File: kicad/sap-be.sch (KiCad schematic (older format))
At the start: 0 parts

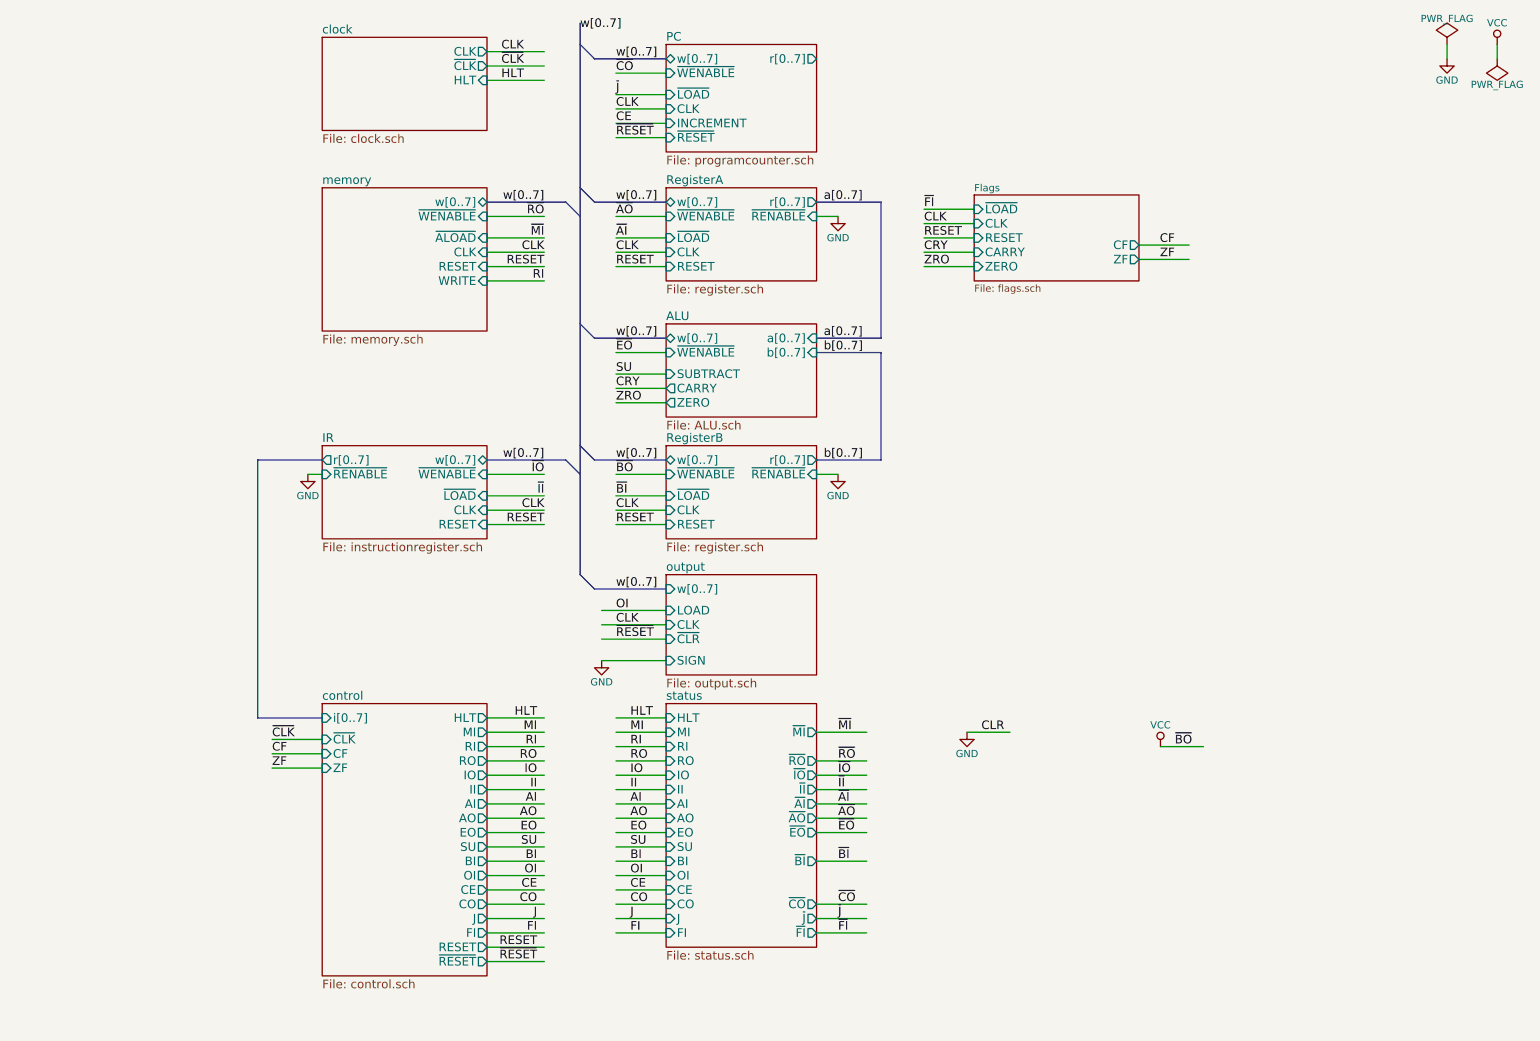
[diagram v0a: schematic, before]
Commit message: Update bugfix version to use updated kicad libraries
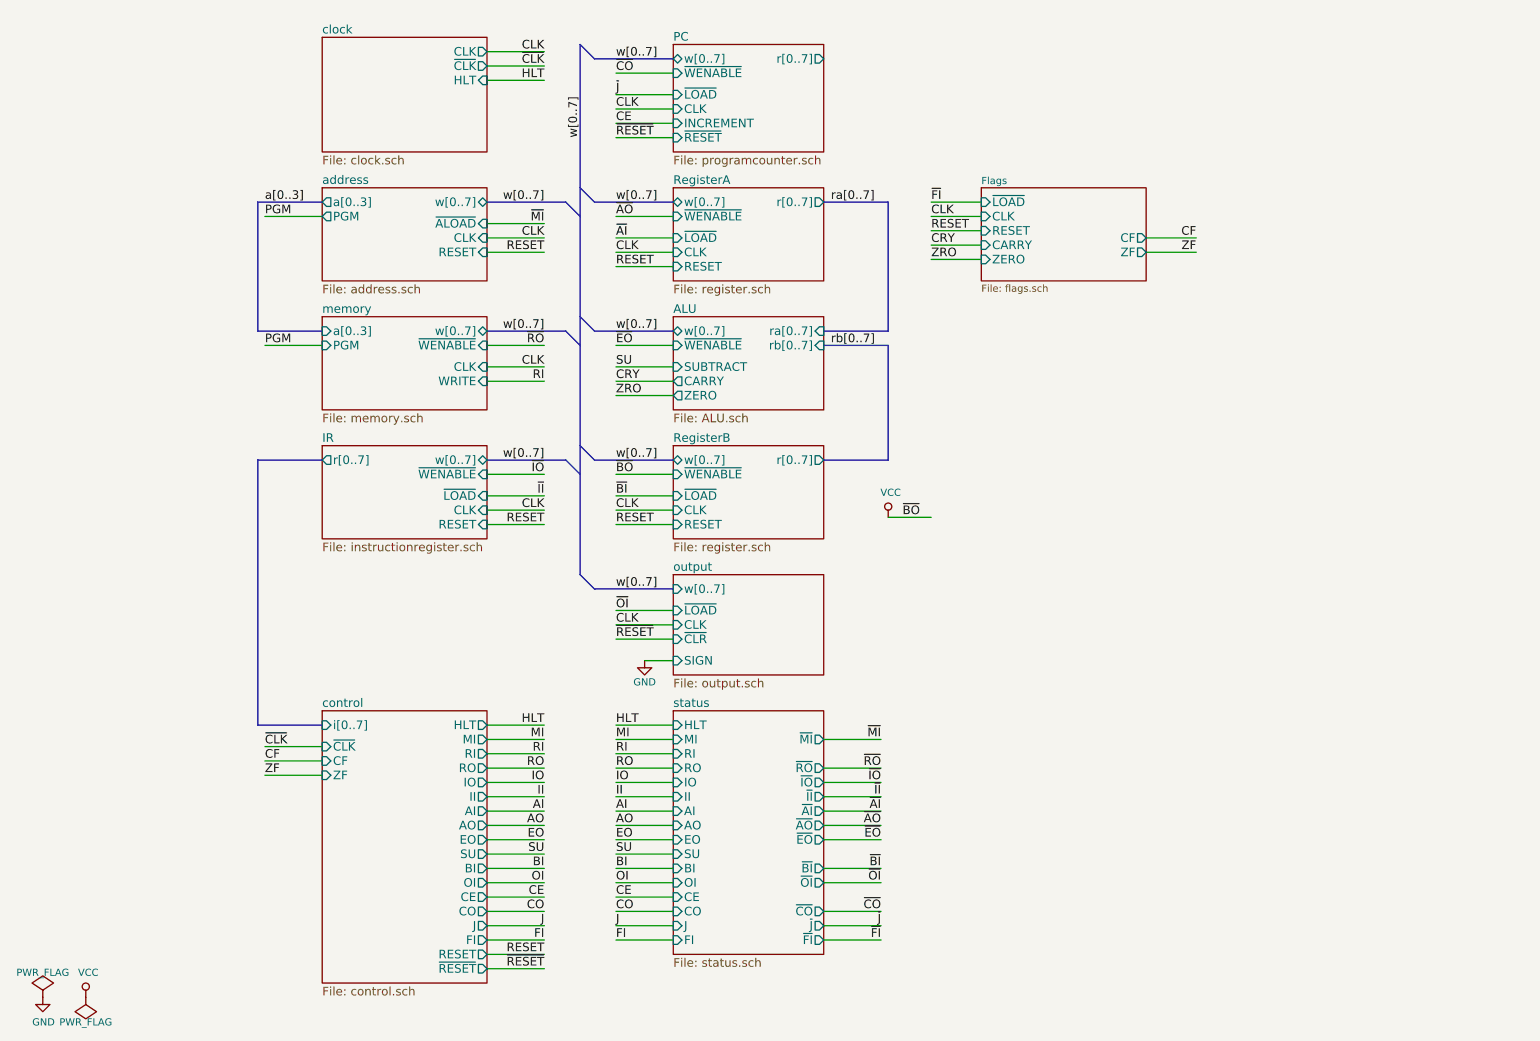
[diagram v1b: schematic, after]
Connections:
- net labels added: PGM, a[0..3], ra[0..7], rb[0..7], ~OI
- net labels removed: CLR, a[0..7], b[0..7]
- wire segments 95 -> 93
